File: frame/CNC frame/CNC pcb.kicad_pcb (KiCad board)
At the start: 2 copper layers, 86 x 86 mm, 0 parts

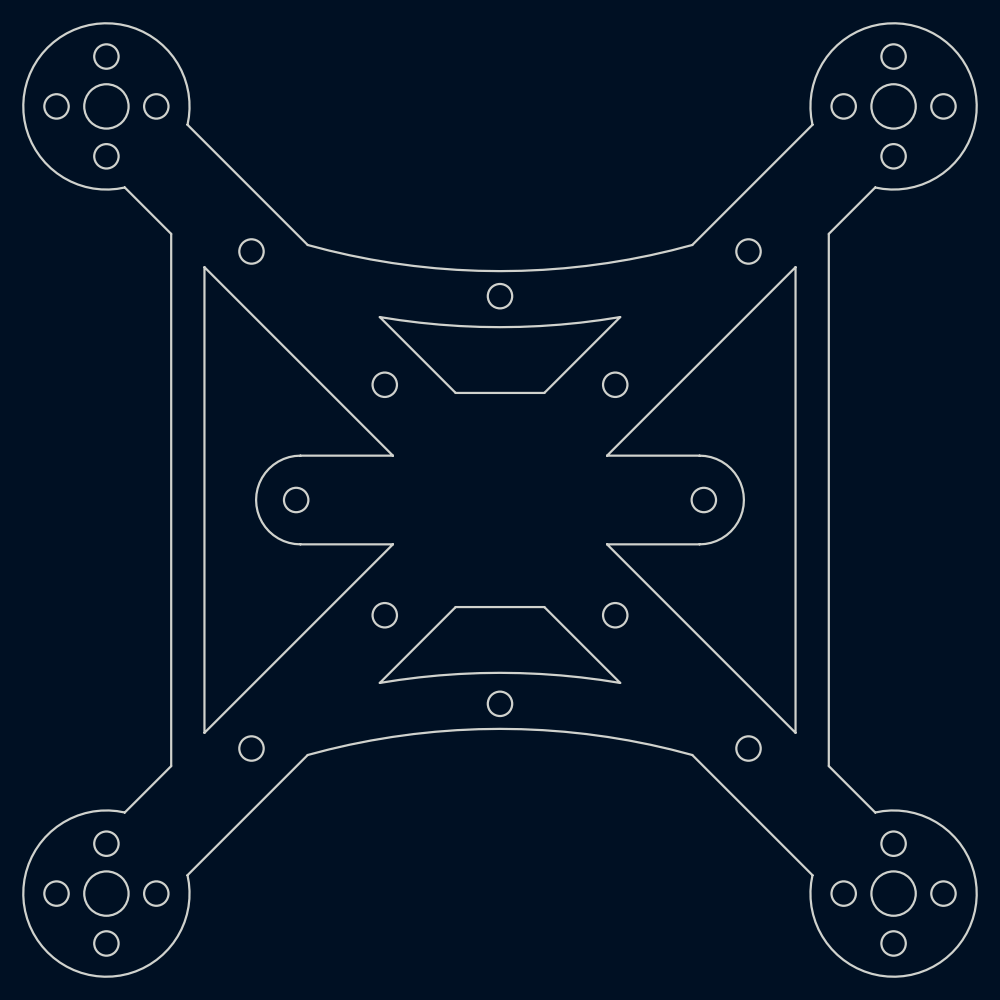
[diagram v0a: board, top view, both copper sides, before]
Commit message: new colord in frame model
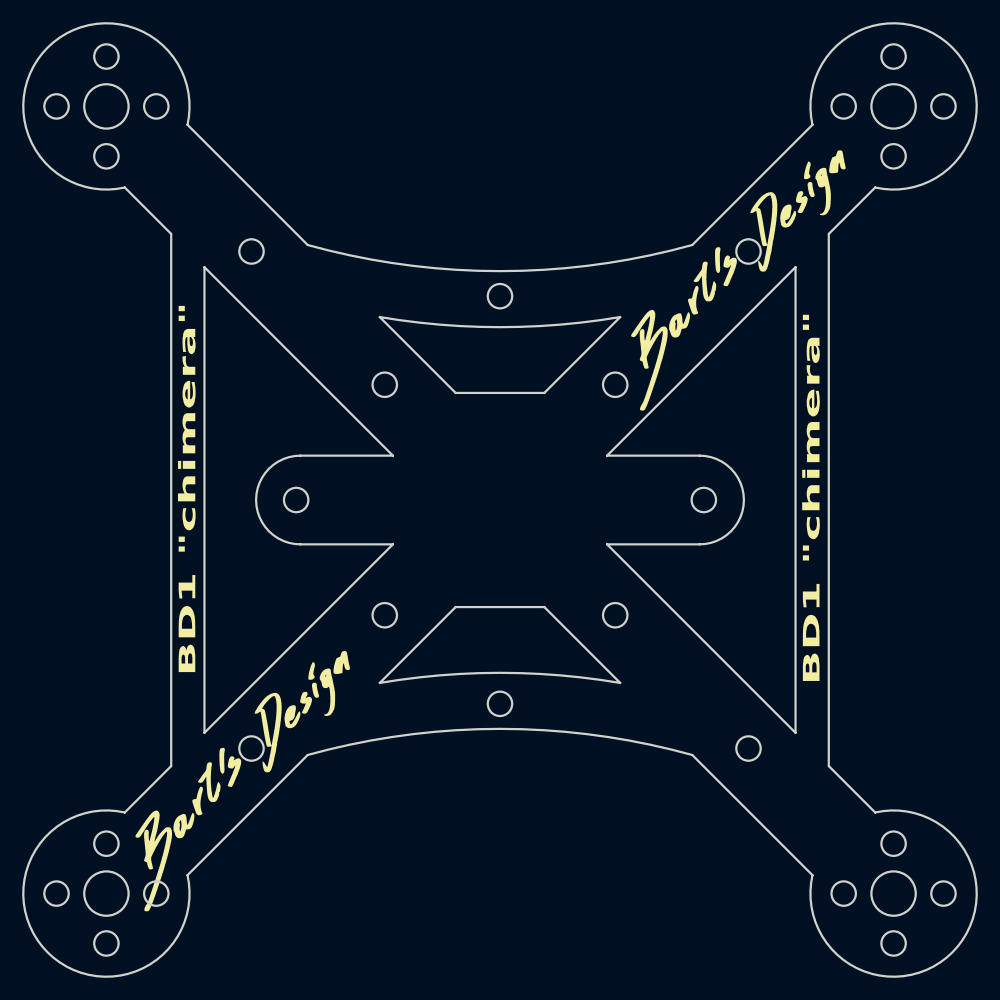
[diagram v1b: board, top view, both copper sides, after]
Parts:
- added REF**: Bart's Design 30mm, BDLib:Bart's Design 30mm, F.Cu at (86.4, 120.0)
- added REF**: Bart's Design 30mm, BDLib:Bart's Design 30mm, F.Cu at (131.1, 74.8)
- added REF**: Bart's Design 30mm, BDLib:Bart's Design 30mm, B.Cu at (131.1, 116.2)
- added REF**: Bart's Design 30mm, BDLib:Bart's Design 30mm, B.Cu at (86.4, 71.1)
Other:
- board text added: "BD1 {dblquote}chimera{dblquote}"
